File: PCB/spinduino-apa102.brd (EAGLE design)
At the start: 79.7 x 88.9 mm, 31 parts, among them U1 MC74VHC1GT125DT, U2 MC74VHC1GT125DT

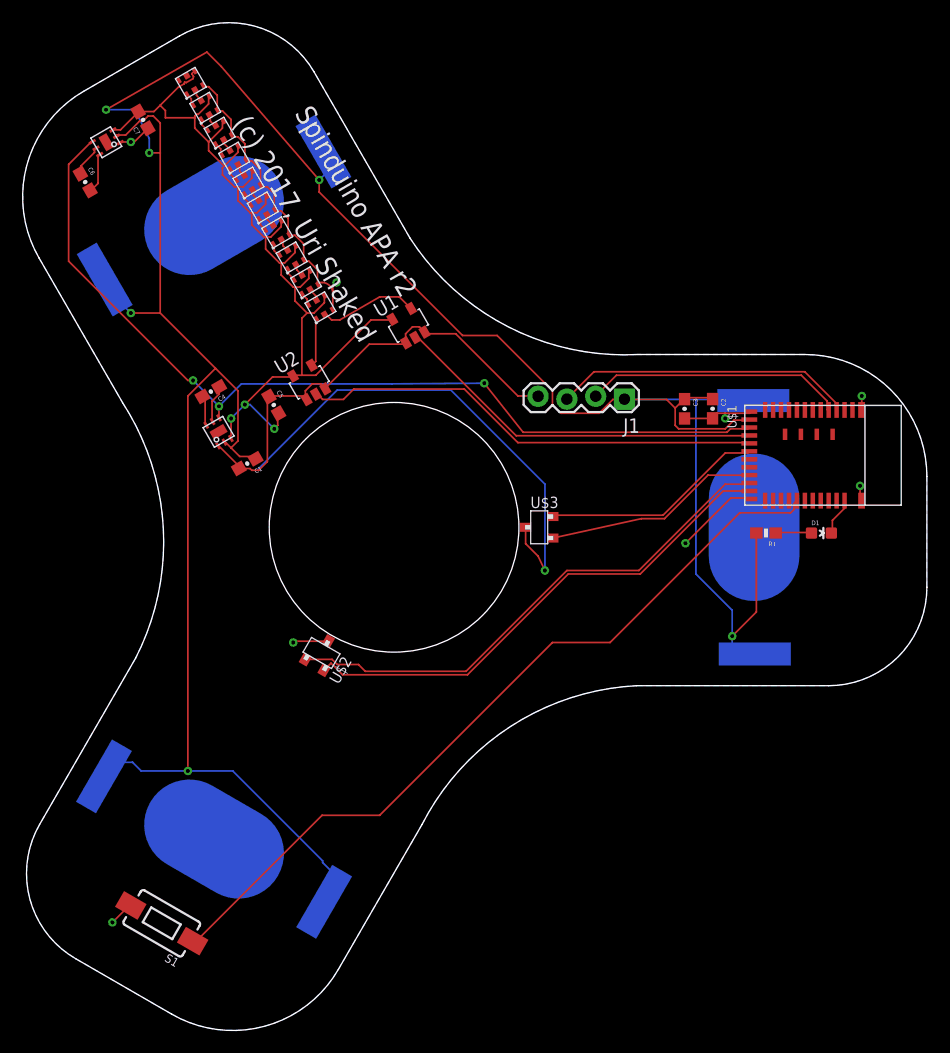
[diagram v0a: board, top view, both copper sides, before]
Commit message: fix a few issues in board:
1. remove copper under antenna
2. fix wrong pin assignments of TPS60150
3. shrink inner hole a bit
4. fix package for MC74VHC1GT125 (SOT353 instead of SOT23-5)
5. move text to a different wing
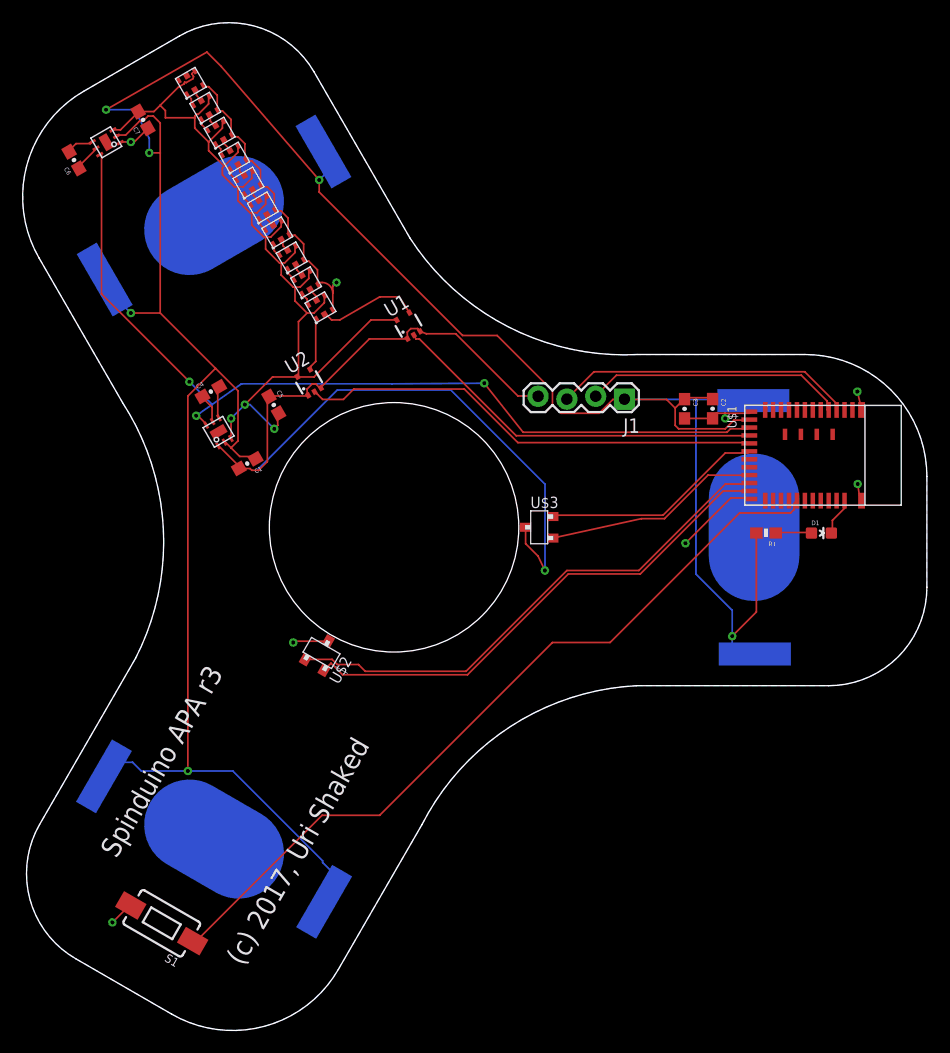
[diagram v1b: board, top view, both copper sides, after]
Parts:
- U1, U2: value MC74VHC1GT125DT -> MC74VHC1GT125DF; device uri:SOT23-5 -> uri:SOT353
- moved C6 2.18 mm to (22.6, 74.3), turned to 120 degrees
- turned C4 to 30 degrees
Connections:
- net LEDS_ENA: now also U$15.6, U$4.6; no longer U$15.4, U$4.4
- net N$22: now also U$4.4; no longer U$4.6
- net N$29: now also U$15.4; no longer U$15.6
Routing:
- net LEDS_ENA: track 80.9 -> 79.5 mm
- net N$29: track 3.58 -> 2.44 mm
- net N$23: track 3.33 -> 2.58 mm
- net 5V: track 87.3 -> 87.9 mm
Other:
- outline, holes or cut-outs redrawn
- board text added: "Spinduino APA r3"
- board text removed: "Spinduino APA r2"

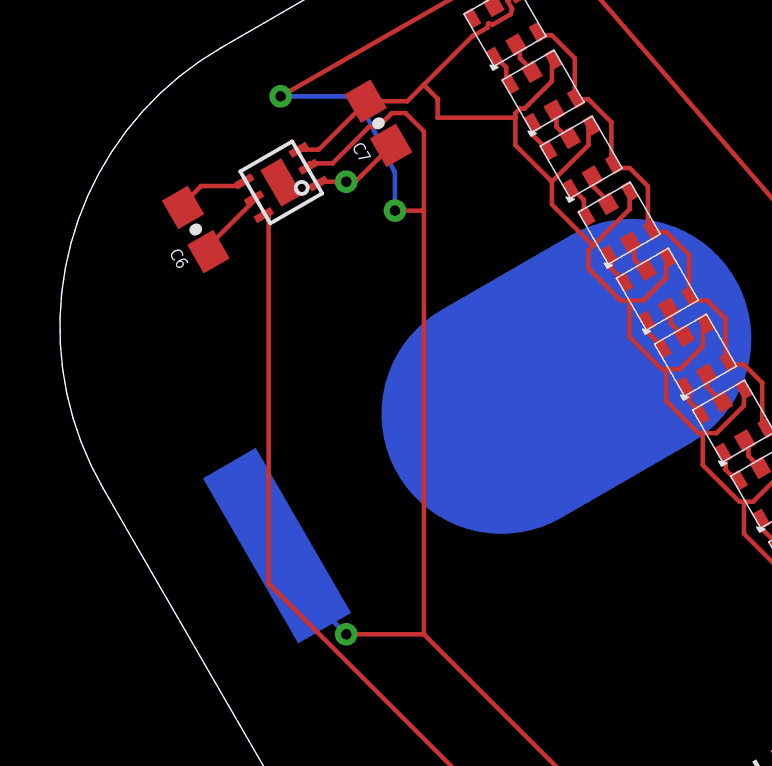
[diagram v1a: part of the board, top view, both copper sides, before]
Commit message: fix: add pull-down resistor for the TPS60150 enable pin
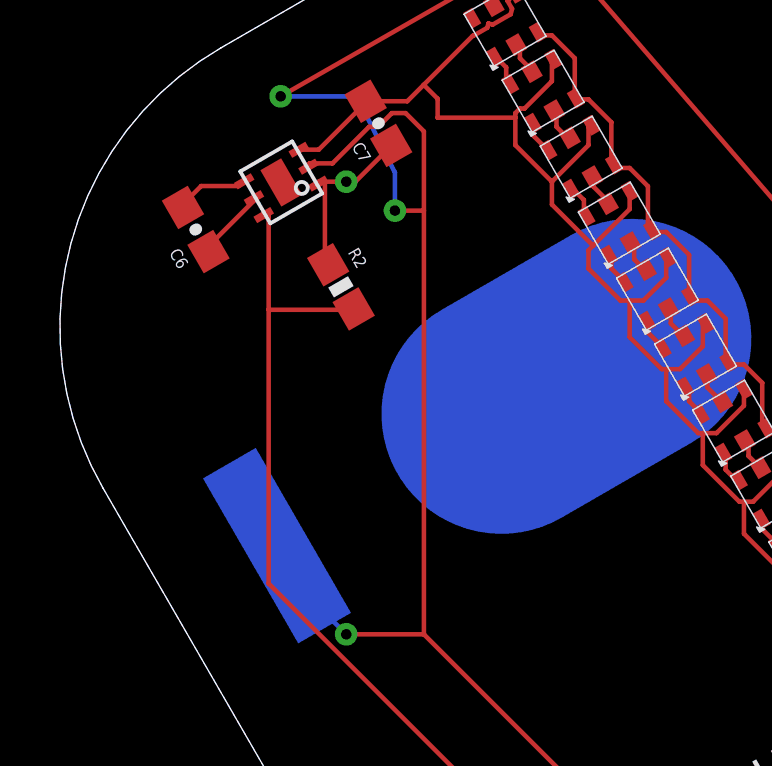
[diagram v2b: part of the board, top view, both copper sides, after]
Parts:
- added R2: 47K, SparkFun-Resistors:0603-RES
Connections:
- net GND: now also R2.1
- net LEDS_ENA: now also R2.2
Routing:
- net GND: track 139.2 -> 142.2 mm
- net LEDS_ENA: track 79.5 -> 82.3 mm
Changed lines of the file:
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@@
 <attribute name="PROD_ID" value="CAP-11015" x="28.66" y="77.84" size="1.778" layer="27" rot="R120" display="off"/>
+</element>
+<element name="R2" library="SparkFun-Resistors" package="0603-RES" value="47K" x="27.41" y="72.39" rot="R300">
+<attribute name="PROD_ID" value="RES-07856" x="27.41" y="72.39" size="1.778" layer="27" rot="R300" display="off"/>
 </element>
 </elements>
@@
 <wire x1="51.9684" y1="58.5216" x2="51.98208125" y2="58.542275" width="0.1524" layer="1"/>
 <wire x1="44.3484" y1="54.2544" x2="44.347915625" y2="54.192275" width="0.1524" layer="1"/>
+<contactref element="R2" pad="1"/>
+<wire x1="26.875" y1="75.875" x2="26.875" y2="73.25" width="0.1524" layer="1"/>
+<wire x1="26.875" y1="73.25" x2="26.985" y2="73.12611875" width="0.1524" layer="1"/>
+<wire x1="26.875" y1="75.875" x2="26.654325" y2="75.83208125" width="0.1524" layer="1"/>
 </signal>
 <signal name="HALL1">
@@
 <wire x1="34.25" y1="51" x2="34.23208125" y2="50.914325" width="0.1524" layer="1"/>
 <wire x1="33.5" y1="51.75" x2="33.3468" y2="51.748" width="0.1524" layer="1"/>
-<wire x1="25" y1="62.5" x2="25" y2="74.75" width="0.1524" layer="1"/>
+<wire x1="25" y1="62.5" x2="25" y2="71.625" width="0.1524" layer="1"/>
+<wire x1="25" y1="71.625" x2="25" y2="74.75" width="0.1524" layer="1"/>
 <wire x1="32.75" y1="54.75" x2="25" y2="62.5" width="0.1524" layer="1"/>
 <wire x1="34.75" y1="52.75" x2="32.75" y2="54.75" width="0.1524" layer="16"/>
@@
 <wire x1="34.75" y1="52.75" x2="34.756428125" y2="52.740871875" width="0.1524" layer="16"/>
 <via x="32.75" y="54.75" extent="1-16" drill="0.35"/>
+<contactref element="R2" pad="2"/>
+<wire x1="25" y1="71.625" x2="27.75" y2="71.625" width="0.1524" layer="1"/>
+<wire x1="27.75" y1="71.625" x2="27.835" y2="71.653878125" width="0.1524" layer="1"/>
 </signal>
 <signal name="N$22">
